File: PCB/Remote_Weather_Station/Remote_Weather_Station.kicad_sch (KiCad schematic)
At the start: 55 parts, among them J101 UART, J102 Stemma_QT_Connector, J103 wire_bus, J104 Servo_Connector, J105 power_in, SW101 SW_Push, SW102 SW_Push, U101 ESP32-WROOM-32D, U102 AD8227, U103 AD8227, U104 AD8227, U105 SIM7600X

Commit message: Add files via upload
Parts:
- added C106, C107, C113, C114: 1u, Capacitor_SMD:C_0805_2012Metric, symbol Device:C_Small
- added R102, R103, R112, R113: 10k, Resistor_SMD:R_0603_1608Metric_Pad0.98x0.95mm_HandSolder, symbol Device:R_Small_US
- renumbered C103 to C102, C104 to C103, C102 to C104, C106 to C108, C107 to C109, C108 to C110, C109 to C111, C110 to C112, C111 to C115, C112 to C116, C113 to C117, C117 to C118, C114 to C119, C115 to C120, C116 to C121, R102 to R104, R103 to R105, R104 to R106, R105 to R107, R106 to R108, R107 to R109, R108 to R110, R109 to R111, R110 to R114, R111 to R115, R112 to R116, R113 to R117, R114 to R118, R115 to R119, R116 to R120, R117 to R121, R121 to R122, R118 to R123, R119 to R124, R120 to R125, U105 to U102, U102 to U103, U103 to U104, U104 to U105
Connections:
- net East_West_Ref: now also C107.1, R103.2; no longer J103.4 (Pin_4), J103.7 (Pin_7)
- net GND: now also J102.MP, C106.2, C107.2, C113.2, C114.2
- net Green_Wire: now also U103.4 (+), C113.1, R112.2; no longer J103.10 (Pin_10), U103.1 (-)
- net North_South_Ref: now also C106.1, R102.2; no longer J103.2 (Pin_2), J103.5 (Pin_5)
- net White_Wire: now also U103.1 (-), C114.1, R113.2; no longer J103.11 (Pin_11), U103.4 (+)
- new net E_red_wire: J103.4 (Pin_4), J103.7 (Pin_7), R103.1
- new net Green_Wire_in: J103.10 (Pin_10), R112.1
- new net N_red_wire: J103.2 (Pin_2), J103.5 (Pin_5), R102.1
- new net White_Wire_in: J103.11 (Pin_11), R113.1
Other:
- note added: "Filter from load cell"
- moved on the sheet: C101, C104, C110, C118, J103, J105, R105, R106, R109, R110

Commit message: Add files via upload
PCB Progress, Layout coming along
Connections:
- net modem_tx: now reaches U101.11 (IO26)
- net modem_tx: now also U102.22 (TXD)
- net modem_rx: now reaches U101.12 (IO27)
- net modem_rx: now also U102.21 (RXD)
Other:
- moved on the sheet: R105, R106, R109, R110

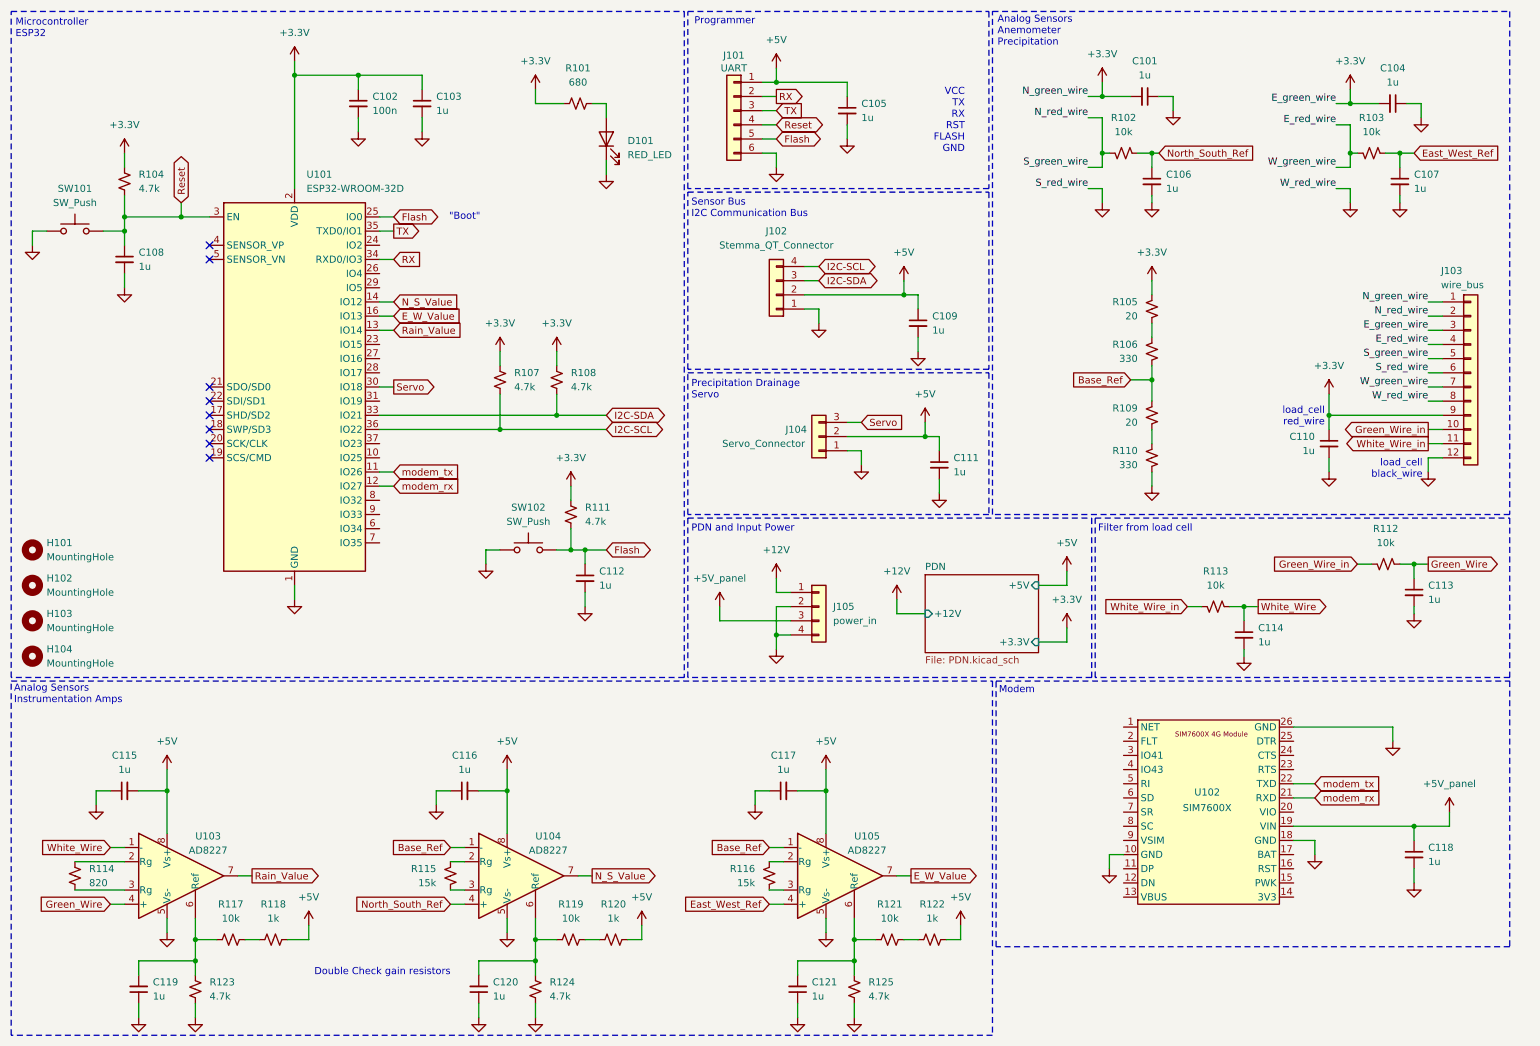
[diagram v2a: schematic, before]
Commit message: Vias
Vias should be added and tied to pads
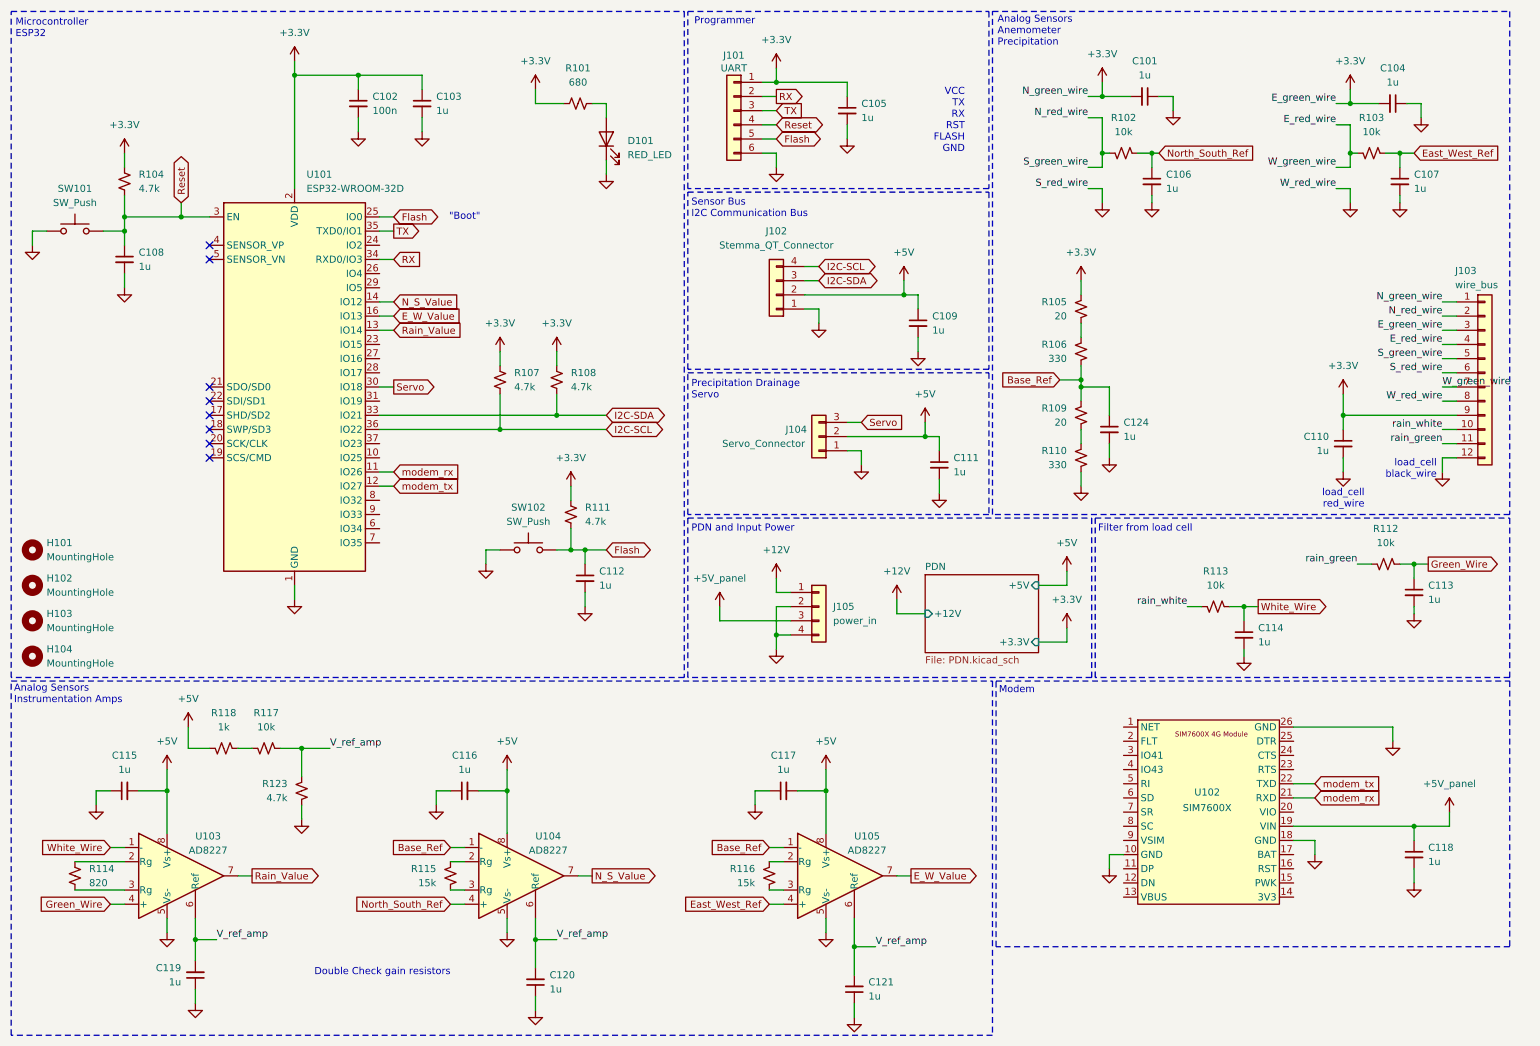
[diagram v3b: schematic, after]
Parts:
- removed R119, R121: 10k, Resistor_SMD:R_0603_1608Metric_Pad0.98x0.95mm_HandSolder, symbol Device:R_Small_US
- removed R120, R122: 1k, Resistor_SMD:R_0603_1608Metric_Pad0.98x0.95mm_HandSolder, symbol Device:R_Small_US
- removed R124, R125: 4.7k, Resistor_SMD:R_0603_1608Metric_Pad0.98x0.95mm_HandSolder, symbol Device:R_Small_US
- added C124: 1u, Capacitor_SMD:C_0805_2012Metric, symbol Device:C_Small
- J104: now left out of the parts list
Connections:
- net +3.3V: now also C105.1, J101.1 (Pin_1)
- net +5V: no longer C105.1, J101.1 (Pin_1)
- net Base_Ref: now also C124.1
- net GND: now also C124.2
- net modem_rx: now also U101.11 (IO26); no longer U101.12 (IO27)
- net modem_tx: now also U101.12 (IO27); no longer U101.11 (IO26)
- net V_ref_amp: now reaches C120.2, U104.6 (Ref)
- net V_ref_amp: now also C119.2, C121.2, R117.2, R123.1, U103.6 (Ref), U105.6 (Ref)
- net Green_Wire_in renamed rain_green
- net rain_green: now also J103.11 (Pin_11); no longer J103.10 (Pin_10)
- net White_Wire_in renamed rain_white
- net rain_white: now also J103.10 (Pin_10); no longer J103.11 (Pin_11)
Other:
- moved on the sheet: C110, C119, C120, C121, J103, R105, R106, R109, R110, R117, R118, R123

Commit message: Add files via upload
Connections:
- net Flash: no longer U101.25 (IO0)
- net Reset: now also U101.25 (IO0)
- net modem_rx: now also U101.12 (IO27); no longer U101.11 (IO26)
- net modem_tx: now also U101.11 (IO26); no longer U101.12 (IO27)
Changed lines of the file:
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@@
 	(wire
 		(pts
-			(xy 80.01 96.52) (xy 82.55 96.52)
-		)
-		(stroke
-			(width 0)
-			(type default)
-		)
-	)
-	(wire
-		(pts
 			(xy 273.05 83.82) (xy 270.51 83.82)
 		)
@@
 	(wire
 		(pts
+			(xy 80.01 96.52) (xy 82.55 96.52)
+		)
+		(stroke
+			(width 0)
+			(type default)
+		)
+	)
+	(wire
+		(pts
 			(xy 92.71 163.83) (xy 95.25 163.83)
 		)
@@
 	(wire
 		(pts
+			(xy 80.01 99.06) (xy 82.55 99.06)
+		)
+		(stroke
+			(width 0)
+			(type default)
+		)
+	)
+	(wire
+		(pts
 			(xy 222.25 29.21) (xy 222.25 31.75)
 		)
@@
 	(wire
 		(pts
-			(xy 80.01 99.06) (xy 82.55 99.06)
-		)
-		(stroke
-			(width 0)
-			(type default)
-		)
-	)
-	(wire
-		(pts
 			(xy 205.74 96.52) (xy 205.74 99.06)
 		)
@@
 	(global_label "modem_rx"
 		(shape input)
-		(at 82.55 96.52 0)
+		(at 82.55 99.06 0)
 		(fields_autoplaced yes)
 		(effects
@@
 		)
 		(property "Intersheetrefs" "${INTERSHEET_REFS}"
-			(at 95.0903 96.52 0)
+			(at 95.0903 99.06 0)
 			(effects
 				(font
@@
 		)
 	)
-	(global_label "Flash"
-		(shape bidirectional)
-		(at 82.55 50.8 0)
-		(fields_autoplaced yes)
-		(effects
-			(font
-				(size 1.27 1.27)
-			)
-			(justify left)
-		)
-		(property "Intersheetrefs" "${INTERSHEET_REFS}"
-			(at 91.7264 50.8 0)
-			(effects
-				(font
-					(size 1.27 1.27)
-				)
-				(justify left)
-				(hide yes)
-			)
-		)
-	)
 	(global_label "N_S_Value"
 		(shape input)
@@
 		)
 	)
+	(global_label "Reset"
+		(shape bidirectional)
+		(at 82.55 50.8 0)
+		(fields_autoplaced yes)
+		(effects
+			(font
+				(size 1.27 1.27)
+			)
+			(justify left)
+		)
+		(property "Intersheetrefs" "${INTERSHEET_REFS}"
+			(at 91.8475 50.8 0)
+			(effects
+				(font
+					(size 1.27 1.27)
+				)
+				(justify left)
+				(hide yes)
+			)
+		)
+	)
 	(global_label "White_Wire"
 		(shape input)
@@
 	(global_label "modem_tx"
 		(shape input)
-		(at 82.55 99.06 0)
+		(at 82.55 96.52 0)
 		(fields_autoplaced yes)
 		(effects
@@
 		)
 		(property "Intersheetrefs" "${INTERSHEET_REFS}"
-			(at 95.0298 99.06 0)
+			(at 95.0298 96.52 0)
 			(effects
 				(font
@@
 		(lib_id "Device:C_Small")
 		(at 176.53 69.85 0)
+		(mirror y)
 		(unit 1)
 		(exclude_from_sim no)
@@
 		(on_board yes)
 		(dnp no)
-		(fields_autoplaced yes)
 		(property "Reference" "C109"
-			(at 179.07 68.5862 0)
+			(at 173.99 68.5862 0)
 			(effects
 				(font
@@
 		)
 		(property "Value" "1u"
-			(at 179.07 71.1262 0)
+			(at 173.99 71.1262 0)
 			(effects
 				(font

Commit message: Add files via upload
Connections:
- net Flash: now also U101.25 (IO0); no longer J101.5 (Pin_5)
- net GND: now also J101.2 (Pin_2); no longer J101.6 (Pin_6)
- net RX: now also J101.3 (Pin_3); no longer J101.2 (Pin_2)
- net Reset: no longer J101.4 (Pin_4), U101.25 (IO0)
- net TX: now also J101.4 (Pin_4); no longer J101.3 (Pin_3)
- no-connect marks 8 -> 10
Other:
- note added: "VCC GND TX RX"
- note removed: "VCC TX RX RST FLASH GND"
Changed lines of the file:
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@@
 		)
 	)
-	(text "VCC\nTX\nRX\nRST\nFLASH\nGND"
+	(text "VCC\nGND\nTX\nRX\n"
 		(exclude_from_sim no)
-		(at 184.912 33.528 0)
+		(at 177.038 29.972 0)
 		(effects
 			(font
@@
 	)
 	(no_connect
+		(at 151.13 39.37)
+	)
+	(no_connect
 		(at 49.53 83.82)
 	)
@@
 		(at 49.53 58.42)
 	)
+	(no_connect
+		(at 151.13 36.83)
+	)
 	(wire
 		(pts
@@
 	(wire
 		(pts
-			(xy 148.59 29.21) (xy 151.13 29.21)
-		)
-		(stroke
-			(width 0)
-			(type default)
-		)
-	)
-	(wire
-		(pts
 			(xy 266.7 30.48) (xy 266.7 33.02)
 		)
@@
 	(wire
 		(pts
+			(xy 148.59 31.75) (xy 151.13 31.75)
+		)
+		(stroke
+			(width 0)
+			(type default)
+		)
+	)
+	(wire
+		(pts
 			(xy 76.2 25.4) (xy 87.63 25.4)
 		)
@@
 	(wire
 		(pts
+			(xy 158.75 29.21) (xy 158.75 35.56)
+		)
+		(stroke
+			(width 0)
+			(type default)
+		)
+	)
+	(wire
+		(pts
 			(xy 205.74 77.47) (xy 205.74 80.01)
 		)
@@
 	(wire
 		(pts
+			(xy 148.59 29.21) (xy 158.75 29.21)
+		)
+		(stroke
+			(width 0)
+			(type default)
+		)
+	)
+	(wire
+		(pts
 			(xy 273.05 81.28) (xy 270.51 81.28)
 		)
@@
 	(wire
 		(pts
-			(xy 151.13 39.37) (xy 151.13 41.91)
-		)
-		(stroke
-			(width 0)
-			(type default)
-		)
-	)
-	(wire
-		(pts
 			(xy 209.55 48.26) (xy 209.55 45.72)
 		)
@@
 	(wire
 		(pts
-			(xy 148.59 31.75) (xy 151.13 31.75)
-		)
-		(stroke
-			(width 0)
-			(type default)
-		)
-	)
-	(wire
-		(pts
 			(xy 92.71 153.67) (xy 90.17 153.67)
 		)
@@
 		)
 	)
-	(global_label "Flash"
-		(shape bidirectional)
-		(at 151.13 36.83 0)
-		(fields_autoplaced yes)
-		(effects
-			(font
-				(size 1.27 1.27)
-			)
-			(justify left)
-		)
-		(property "Intersheetrefs" "${INTERSHEET_REFS}"
-			(at 160.3064 36.83 0)
-			(effects
-				(font
-					(size 1.27 1.27)
-				)
-				(justify left)
-				(hide yes)
-			)
-		)
-	)
 	(global_label "TX"
 		(shape input)
-		(at 151.13 31.75 0)
+		(at 151.13 34.29 0)
 		(fields_autoplaced yes)
 		(effects
@@
 		)
 		(property "Intersheetrefs" "${INTERSHEET_REFS}"
-			(at 156.2923 31.75 0)
+			(at 156.2923 34.29 0)
 			(effects
 				(font
@@
 		)
 	)
-	(global_label "Reset"
-		(shape bidirectional)
-		(at 82.55 50.8 0)
-		(fields_autoplaced yes)
-		(effects
-			(font
-				(size 1.27 1.27)
-			)
-			(justify left)
-		)
-		(property "Intersheetrefs" "${INTERSHEET_REFS}"
-			(at 91.8475 50.8 0)
-			(effects
-				(font
-					(size 1.27 1.27)
-				)
-				(justify left)
-				(hide yes)
-			)
-		)
-	)
 	(global_label "White_Wire"
 		(shape input)
@@
 		)
 	)
-	(global_label "Reset"
-		(shape bidirectional)
-		(at 151.13 34.29 0)
+	(global_label "TX"
+		(shape output)
+		(at 82.55 53.34 0)
 		(fields_autoplaced yes)
 		(effects
@@
 		)
 		(property "Intersheetrefs" "${INTERSHEET_REFS}"
-			(at 160.4275 34.29 0)
+			(at 87.7123 53.34 0)
 			(effects
 				(font
@@
 		)
 	)
-	(global_label "TX"
-		(shape output)
-		(at 82.55 53.34 0)
+	(global_label "Rain_Value"
+		(shape input)
+		(at 82.55 71.12 0)
 		(fields_autoplaced yes)
 		(effects
@@
 		)
 		(property "Intersheetrefs" "${INTERSHEET_REFS}"
-			(at 87.7123 53.34 0)
+			(at 95.816 71.12 0)
 			(effects
 				(font
@@
 		)
 	)
-	(global_label "Rain_Value"
-		(shape input)
-		(at 82.55 71.12 0)
+	(global_label "I2C-SCL"
+		(shape bidirectional)
+		(at 120.65 88.9 0)
 		(fields_autoplaced yes)
 		(effects
@@
 		)
 		(property "Intersheetrefs" "${INTERSHEET_REFS}"
-			(at 95.816 71.12 0)
+			(at 132.9108 88.9 0)
 			(effects
 				(font
@@
 		)
 	)
-	(global_label "I2C-SCL"
+	(global_label "Flash"
 		(shape bidirectional)
-		(at 120.65 88.9 0)
+		(at 82.55 50.8 0)
 		(fields_autoplaced yes)
 		(effects
@@
 		)
 		(property "Intersheetrefs" "${INTERSHEET_REFS}"
-			(at 132.9108 88.9 0)
+			(at 91.7264 50.8 0)
 			(effects
 				(font
@@
 	(global_label "RX"
 		(shape output)
-		(at 151.13 29.21 0)
+		(at 151.13 31.75 0)
 		(fields_autoplaced yes)
 		(effects
@@
 		)
 		(property "Intersheetrefs" "${INTERSHEET_REFS}"
-			(at 156.5947 29.21 0)
+			(at 156.5947 31.75 0)
 			(effects
 				(font
@@
 	(symbol
 		(lib_id "power:GND")
+		(at 158.75 35.56 0)
+		(unit 1)
+		(exclude_from_sim no)
+		(in_bom yes)
+		(on_board yes)
+		(dnp no)
+		(fields_autoplaced yes)
+		(property "Reference" "#PWR0112"
+			(at 158.75 41.91 0)
+			(effects
+				(font
+					(size 1.27 1.27)
+				)
+				(hide yes)
+			)
+		)
+		(property "Value" "GND"
+			(at 158.75 40.64 0)
+			(effects
+				(font
+					(size 1.27 1.27)
+				)
+				(hide yes)
+			)
+		)
+		(property "Footprint" ""
+			(at 158.75 35.56 0)
+			(effects
+				(font
+					(size 1.27 1.27)
+				)
+				(hide yes)
+			)
+		)
+		(property "Datasheet" ""
+			(at 158.75 35.56 0)
+			(effects
+				(font
+					(size 1.27 1.27)
+				)
+				(hide yes)
+			)
+		)
+		(property "Description" "Power symbol creates a global label with name \"GND\" , ground"
+			(at 158.75 35.56 0)
+			(effects
+				(font
+					(size 1.27 1.27)
+				)
+				(hide yes)
+			)
+		)
+		(pin "1"
+		)
+		(instances
+			(project "Remote_Weather_Station"
+				(path "/a9f3e948-f0cb-4784-bed2-bdf72b5832ff"
+					(reference "#PWR0112")
+					(unit 1)
+				)
+			)
+		)
+	)
+	(symbol
+		(lib_id "power:GND")
 		(at 102.87 179.07 0)
 		(unit 1)
@@
 					(unit 1)
 				)
-			)
-		)
-	)
-	(symbol
-		(lib_id "power:GND")
-		(at 151.13 41.91 0)
-		(unit 1)
-		(exclude_from_sim no)
-		(in_bom yes)
-		(on_board yes)
-		(dnp no)
-		(fields_autoplaced yes)
-		(property "Reference" "#PWR0112"
-			(at 151.13 48.26 0)
-			(effects
-				(font
-					(size 1.27 1.27)
-				)
-				(hide yes)
-			)
-		)
-		(property "Value" "GND"
-			(at 151.13 46.99 0)
-			(effects
-				(font
-					(size 1.27 1.27)
-				)
-				(hide yes)
-			)
-		)
-		(property "Footprint" ""
-			(at 151.13 41.91 0)
-			(effects
-				(font
-					(size 1.27 1.27)
-				)
-				(hide yes)
-			)
-		)
-		(property "Datasheet" ""
-			(at 151.13 41.91 0)
-			(effects
-				(font
-					(size 1.27 1.27)
-				)
-				(hide yes)
-			)
-		)
-		(property "Description" "Power symbol creates a global label with name \"GND\" , ground"
-			(at 151.13 41.91 0)
-			(effects
-				(font
-					(size 1.27 1.27)
-				)
-				(hide yes)
-			)
-		)
-		(pin "1"
-		)
-		(instances
-			(project "Remote_Weather_Station"
-				(path "/a9f3e948-f0cb-4784-bed2-bdf72b5832ff"
-					(reference "#PWR0112")
-					(unit 1)
-				)
